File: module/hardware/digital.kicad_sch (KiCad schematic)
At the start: 35 parts, among them J10 Conn_01x03, J11 Conn_01x03, J12 Conn_01x03, J5 Conn_01x03_Male, J6 Conn_01x03_Male, J7 Conn_01x03, J8 Conn_01x03, J9 Conn_01x05_Male, SW2 SW_Push, U8 W25Q128JVS, U9 RP2040, Y1 12MHz 18pF

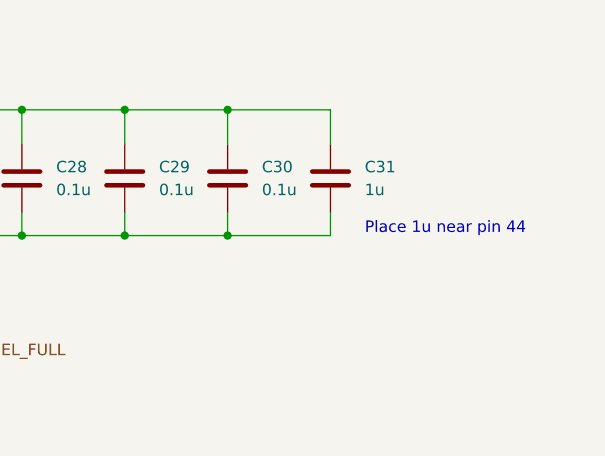
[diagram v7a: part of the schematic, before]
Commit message: Complete board layout component placement & outline approx
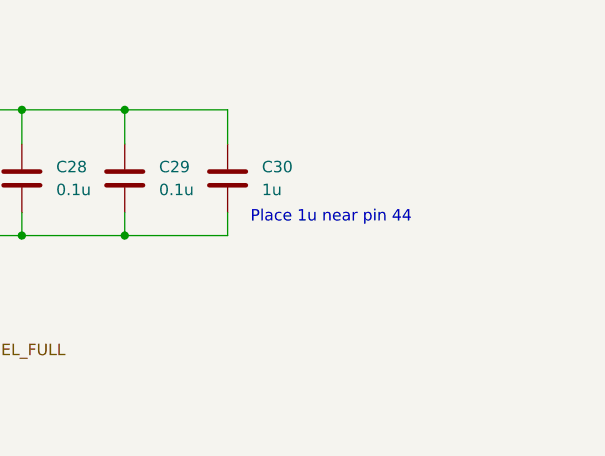
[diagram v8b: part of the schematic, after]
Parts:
- removed C31: 1u, Capacitor_SMD:C_0603_1608Metric_Pad1.08x0.95mm_HandSolder, symbol Device:C
- C30: value 0.1u -> 1u
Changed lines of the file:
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@@
   (junction (at 307.34 54.61) (diameter 0) (color 0 0 0 0)
   )
-  (junction (at 353.06 40.64) (diameter 0) (color 0 0 0 0)
-  )
   (junction (at 270.51 40.64) (diameter 0) (color 0 0 0 0)
   )
@@
   )
   (junction (at 90.17 144.78) (diameter 0) (color 0 0 0 0)
-  )
-  (junction (at 353.06 54.61) (diameter 0) (color 0 0 0 0)
   )
   (junction (at 78.74 144.78) (diameter 0) (color 0 0 0 0)
@@
     (stroke (width 0) (type default) (color 0 0 0 0))
   )
-  (wire (pts (xy 364.49 54.61) (xy 353.06 54.61))
-    (stroke (width 0) (type default) (color 0 0 0 0))
-  )
   (wire (pts (xy 341.63 52.07) (xy 341.63 54.61))
     (stroke (width 0) (type default) (color 0 0 0 0))
@@
     (stroke (width 0) (type default) (color 0 0 0 0))
   )
-  (wire (pts (xy 364.49 40.64) (xy 353.06 40.64))
-    (stroke (width 0) (type default) (color 0 0 0 0))
-  )
   (wire (pts (xy 114.3 147.32) (xy 127 147.32))
     (stroke (width 0) (type default) (color 0 0 0 0))
@@
     (stroke (width 0) (type default) (color 0 0 0 0))
   )
-  (wire (pts (xy 364.49 52.07) (xy 364.49 54.61))
-    (stroke (width 0) (type default) (color 0 0 0 0))
-  )
   (wire (pts (xy 106.68 218.44) (xy 115.57 218.44))
     (stroke (width 0) (type default) (color 0 0 0 0))
@@
   )
   (wire (pts (xy 242.57 90.17) (xy 233.68 90.17))
-    (stroke (width 0) (type default) (color 0 0 0 0))
-  )
-  (wire (pts (xy 364.49 44.45) (xy 364.49 40.64))
     (stroke (width 0) (type default) (color 0 0 0 0))
   )
@@
     (effects (font (size 1.27 1.27)) (justify left bottom))
   )
-  (text "Place 1u near pin 44" (at 368.3 54.61 0)
+  (text "Place 1u near pin 44" (at 355.6 53.34 0)
     (effects (font (size 1.27 1.27)) (justify left bottom))
   )
@@
       (effects (font (size 1.27 1.27)) (justify left))
     )
-    (property "Value" "0.1u" (id 1) (at 356.87 49.5299 0)
+    (property "Value" "1u" (id 1) (at 356.87 49.5299 0)
       (effects (font (size 1.27 1.27)) (justify left))
     )
@@
       (effects (font (size 1.27 1.27)) hide)
     )
-    (pin "1")
-    (pin "2")
-  )
-  (symbol (lib_id "Device:C") (at 364.49 48.26 0) (unit 1)
-    (in_bom yes) (on_board yes) (fields_autoplaced)
-    (property "Reference" "C31" (id 0) (at 368.3 46.9899 0)
-      (effects (font (size 1.27 1.27)) (justify left))
-    )
-    (property "Value" "1u" (id 1) (at 368.3 49.5299 0)
-      (effects (font (size 1.27 1.27)) (justify left))
-    )
-    (property "Footprint" "Capacitor_SMD:C_0603_1608Metric_Pad1.08x0.95mm_HandSolder" (id 2) (at 365.4552 52.07 0)
-      (effects (font (size 1.27 1.27)) hide)
-    )
-    (property "Datasheet" "~" (id 3) (at 364.49 48.26 0)
-      (effects (font (size 1.27 1.27)) hide)
-    )
